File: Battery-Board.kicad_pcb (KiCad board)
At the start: 2 copper layers, 100 x 100 mm, 174 parts, among them J12 USB_C_Receptacle_USB2.0_16P, J13 STM32-Prog-Header, Q1 CSD18563Q5A, Q2 CSD18563Q5A, Q3 CSD18563Q5A, SW3 RESET, SW4 SW_SPDT, U1 8MHz, U10 NTMFS4D0N08XT1G, U11 NTMFS4D0N08XT1G, U12 NTMFS4D0N08XT1G, U13 NTMFS4D0N08XT1G, U14 NTMFS4D0N08XT1G, U23 ACS723xLCTR-10AU, U24 ACS723xLCTR-10AU, U25 MCP6007, U26 MCP6007, U27 ACS723xLCTR-10AU, U28 MCP6007, U29 MCP6007, U3 STM32G491KEUx, U30 MCP6007, U31 MCP6007, U4 MCP2542FD-E/SN, U5 MCP9700AT-ETT, U6 MCP9700AT-ETT, U7 MCP9700AT-ETT

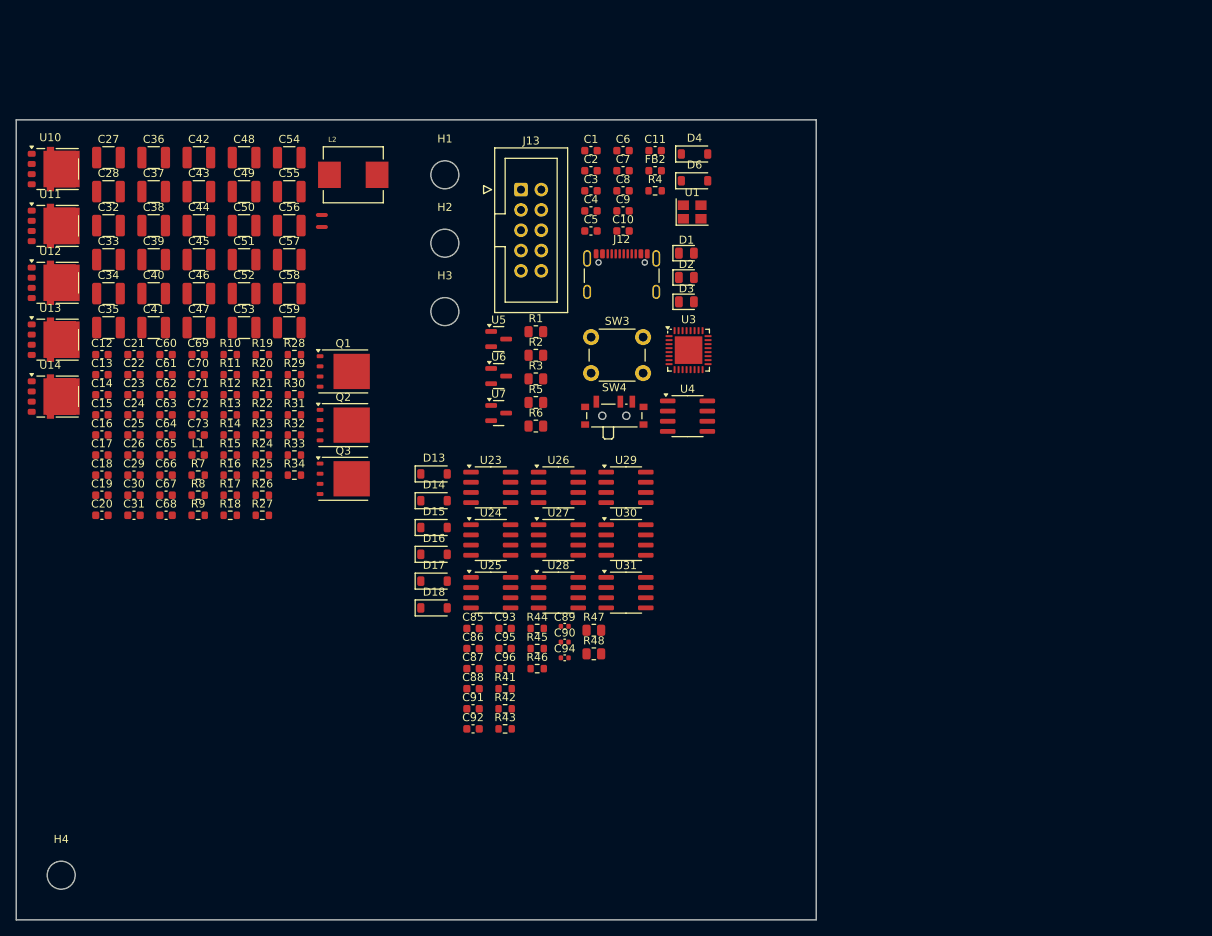
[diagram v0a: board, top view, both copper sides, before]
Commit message: Added missing symbols
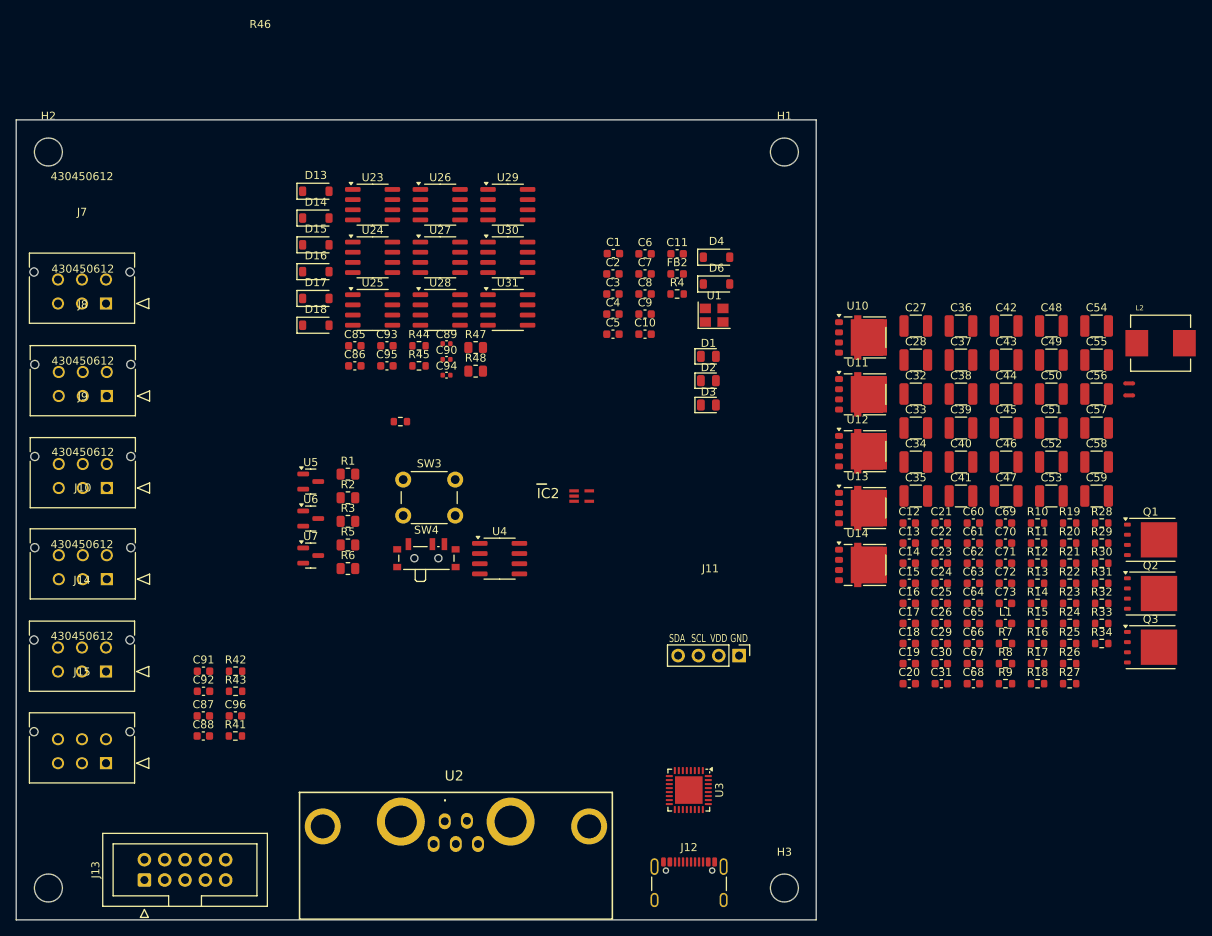
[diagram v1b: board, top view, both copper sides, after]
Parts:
- added IC2: ESDALC6V1W5, ecocad_lib_footprints:SOT65P210X110-5N, F.Cu at (158.6, 90.7)
- added J10: STD_PWR_HEADER, ecocad_lib_footprints:CON_430450612_MOL, F.Cu at (99.2, 101.1)
- added J11: OLED, ecocad_lib_footprints:Display_128x64_096_I2C, F.Cu at (174.4, 110.6)
- added J14: STD_PWR_HEADER, ecocad_lib_footprints:CON_430450612_MOL, F.Cu at (99.1, 112.6)
- added J15: STD_PWR_HEADER, ecocad_lib_footprints:CON_430450612_MOL, F.Cu at (99.1, 124.1)
- added J7: STD_PWR_HEADER, ecocad_lib_footprints:CON_430450612_MOL, F.Cu at (99.1, 66.6)
- added J8: STD_PWR_HEADER, ecocad_lib_footprints:CON_430450612_MOL, F.Cu at (99.2, 78.2)
- added J9: STD_PWR_HEADER, ecocad_lib_footprints:CON_430450612_MOL, F.Cu at (99.2, 89.7)
- added U2: ~, ecocad_lib_footprints:DB7W2-Male, F.Cu at (142.8, 133.0)
- moved L2 103.1 mm to (230.9, 71.6)
- moved Q1 103.1 mm to (229.7, 96.2)
- moved Q2 103.1 mm to (229.7, 102.9)
- moved Q3 103.1 mm to (229.7, 109.6)
- moved C42 103.1 mm to (211.6, 69.5)
- moved C43 103.1 mm to (211.6, 73.7)
- moved C44 103.1 mm to (211.6, 78.0)
- moved C45 103.1 mm to (211.6, 82.2)
- moved C46 103.1 mm to (211.6, 86.5)
- moved C47 103.1 mm to (211.6, 90.7)
- moved C48 103.1 mm to (217.3, 69.5)
- moved C49 103.1 mm to (217.3, 73.7)
- moved C50 103.1 mm to (217.3, 78.0)
- moved C51 103.1 mm to (217.3, 82.2)
- moved C52 103.1 mm to (217.3, 86.5)
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
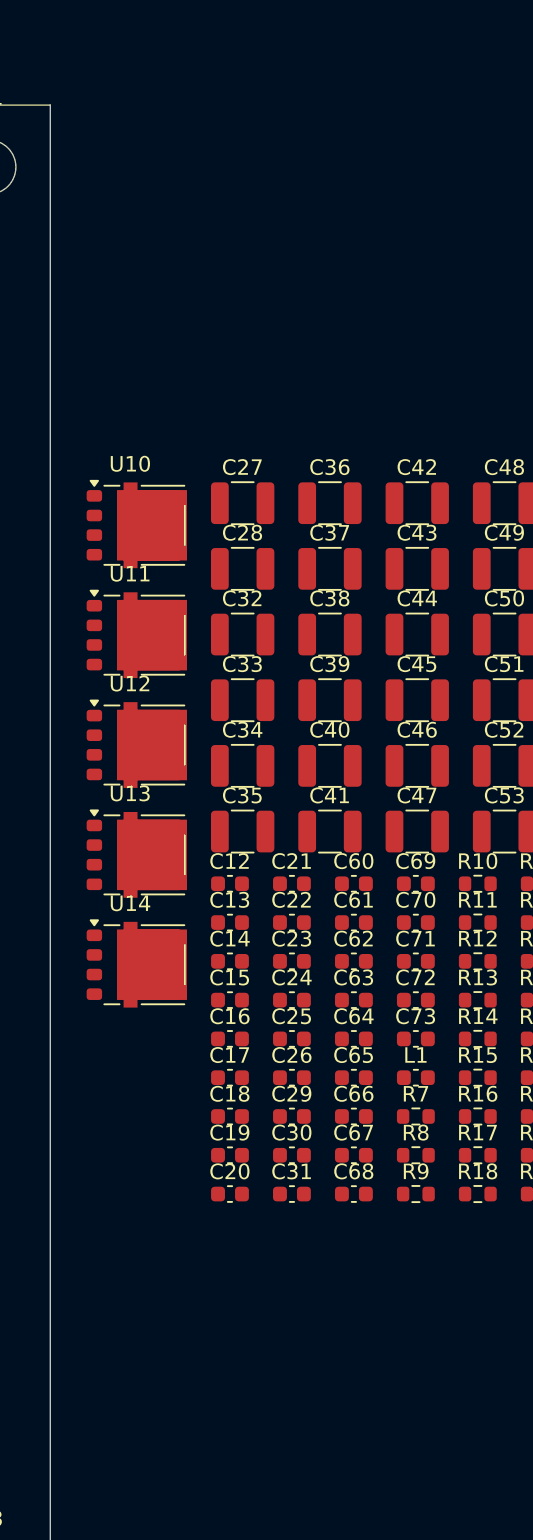
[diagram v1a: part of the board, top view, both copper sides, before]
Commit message: updated footprints for bucks and placement
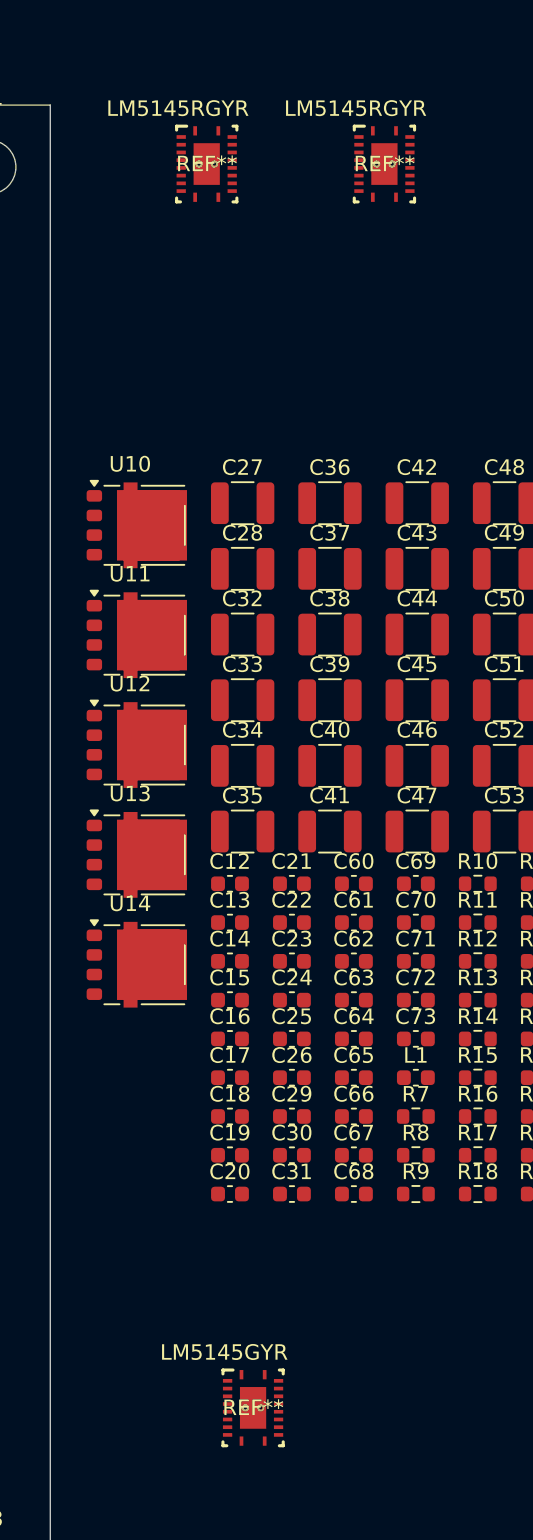
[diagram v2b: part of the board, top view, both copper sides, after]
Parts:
- added REF**: RGY0020B, ecocad_lib_footprints:RGY0020B, F.Cu at (201.0, 128.0)
- added REF**: RGY0020B, RGY0020B, F.Cu at (209.5, 47.5)
- added REF**: RGY0020B, RGY0020B, F.Cu at (198.0, 47.5)

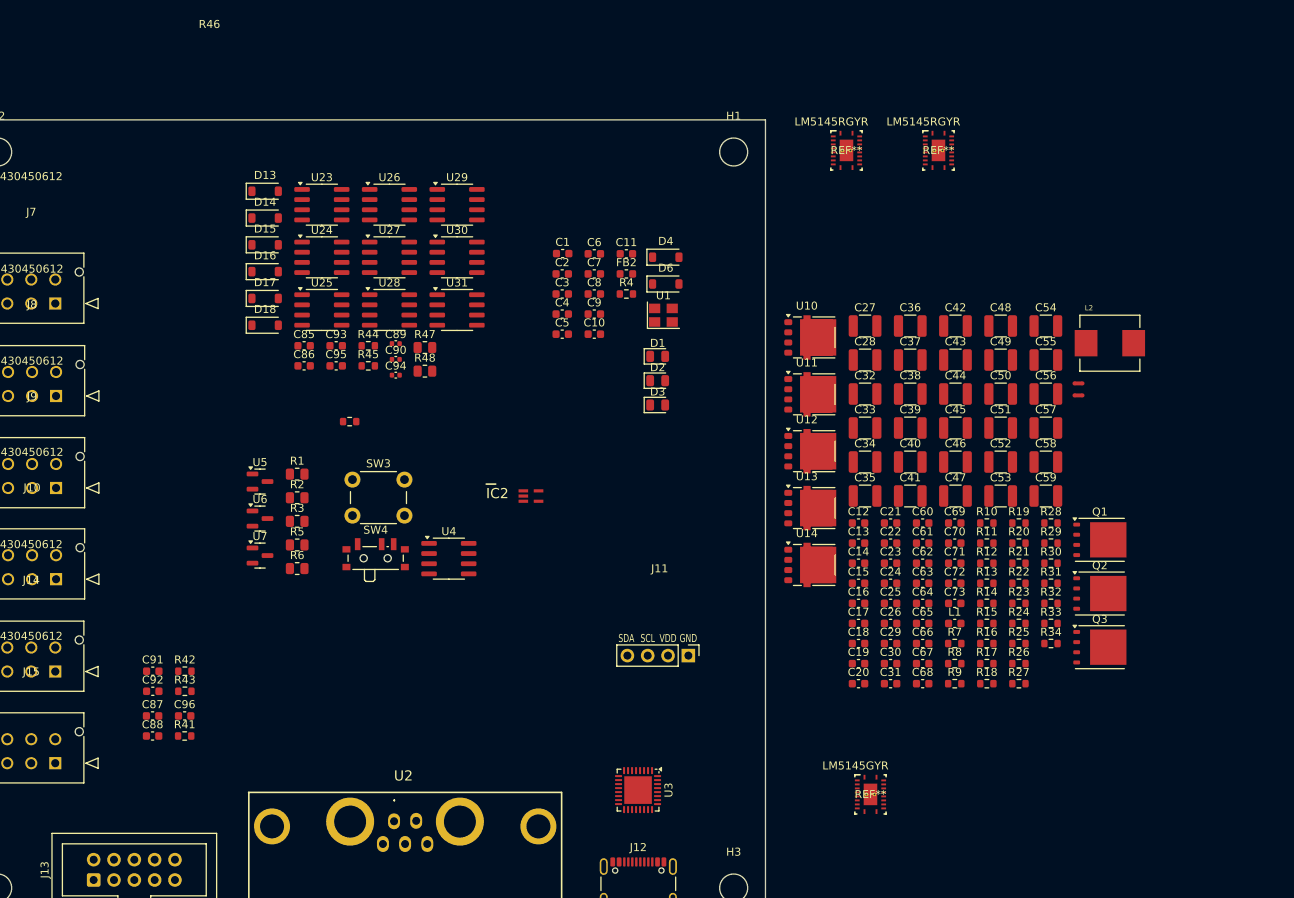
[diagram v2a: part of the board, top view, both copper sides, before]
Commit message: fixed footprints
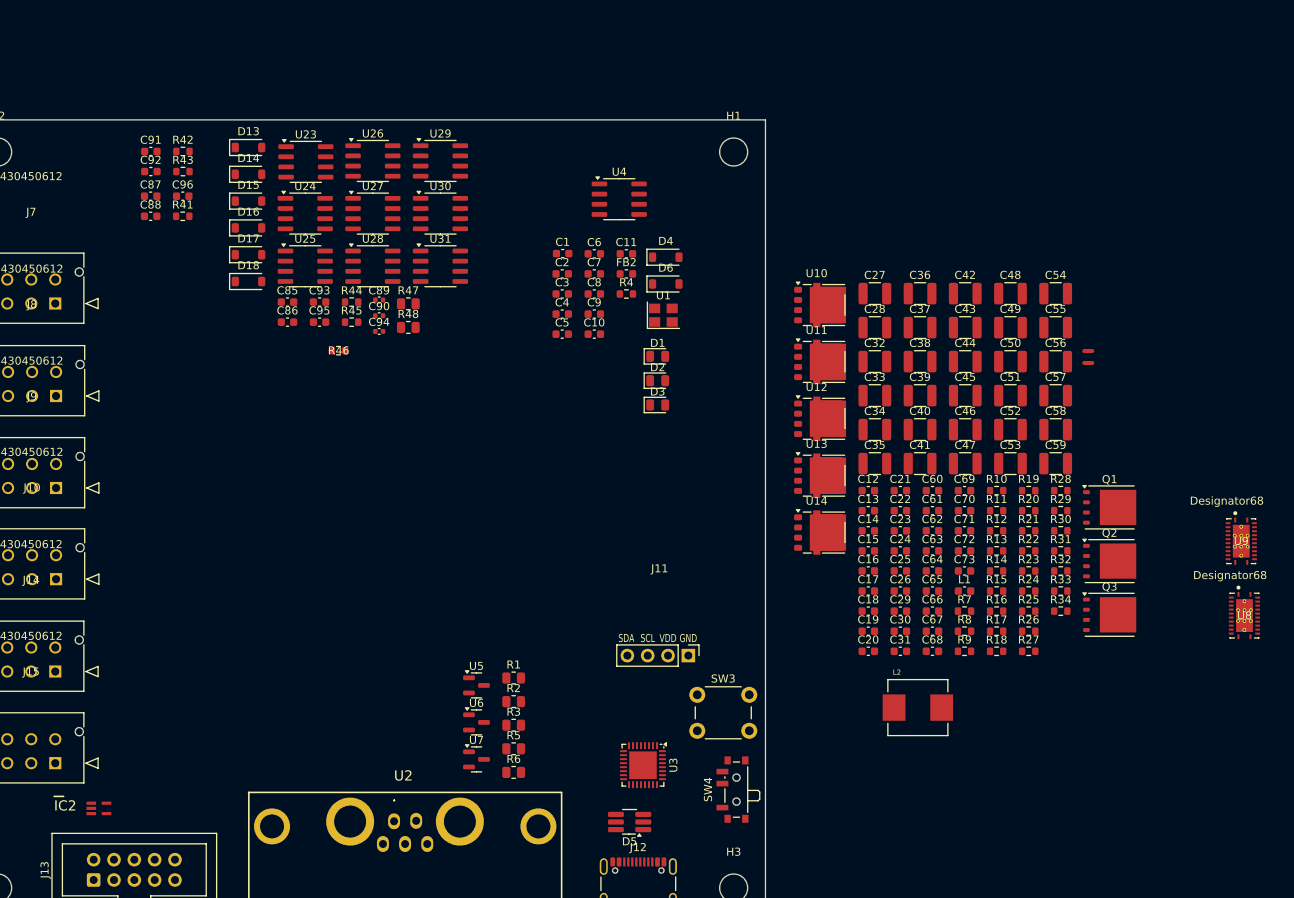
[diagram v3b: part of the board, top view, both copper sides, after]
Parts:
- removed REF**: RGY0020B, ecocad_lib_footprints:RGY0020B
- removed REF** (x2): RGY0020B, RGY0020B
- added D5: USBLC6-2SC6, Package_TO_SOT_SMD:TSOT-23-6_HandSoldering, F.Cu at (170.9, 131.4)
- added U8: LM5145, ecocad_lib_footprints:RGY0024F-MFG, F.Cu at (247.7, 105.7)
- added U9: LM5145, ecocad_lib_footprints:RGY0024F-MFG, F.Cu at (247.3, 96.4)
- moved IC2 66.6 mm to (104.5, 129.8)
- moved C87 65.0 mm to (111.0, 53.2)
- moved C88 65.0 mm to (111.0, 55.7)
- moved C91 65.0 mm to (111.0, 47.6)
- moved C92 65.0 mm to (111.0, 50.1)
- moved C96 65.0 mm to (115.0, 53.2)
- moved R41 65.0 mm to (115.0, 55.7)
- moved R42 65.0 mm to (115.1, 47.6)
- moved R43 65.0 mm to (115.1, 50.1)
- moved SW4 53.5 mm to (183.9, 127.4), turned to 90 degrees
- moved L2 51.5 mm to (206.9, 117.2)
- moved SW3 50.8 mm to (179.3, 115.5)
- moved U4 49.7 mm to (169.6, 53.6)
- moved R1 37.2 mm to (156.4, 113.5)
- moved R2 37.2 mm to (156.4, 116.4)
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
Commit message: updates on pcb layout
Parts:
- removed J10, J14, J15, J7, J8, J9: STD_PWR_HEADER, ecocad_lib_footprints:CON_430450612_MOL
- removed Q3: CSD18563Q5A, Package_TO_SOT_SMD:TDSON-8-1
- added U12: NTMFS4D0N08XT1G, ecocad_lib_footprints:PowerMosDFNHybrid, F.Cu at (155.5, 72.8)
- L1: footprint Capacitor_SMD:C_0603_1608Metric -> ecocad_lib_footprints:L_Bourns_SRR1208_12.7x12.7mm
- L2: footprint ecocad_lib_footprints:IND_SPM7054VC-220M-D -> ecocad_lib_footprints:L_Bourns_SRR1208_12.7x12.7mm
- U2: footprint ecocad_lib_footprints:DB7W2-Male -> ecocad_lib_footprints:DB7W2-30A
- moved U8 149.7 mm to (99.7, 82.9), turned to -90 degrees
- moved R1 142.4 mm to (34.6, 39.7)
- moved R2 142.4 mm to (34.6, 42.6)
- moved R3 142.4 mm to (34.6, 45.6)
- moved R5 142.4 mm to (34.6, 48.5)
- moved R6 142.4 mm to (34.6, 51.5)
- moved U5 142.4 mm to (29.9, 40.6)
- moved U6 142.4 mm to (29.9, 45.2)
- moved U7 142.4 mm to (29.9, 49.9)
- moved D5 139.1 mm to (36.8, 94.5)
- moved C54 119.5 mm to (110.5, 102.2), turned to 180 degrees
- moved C58 118.4 mm to (108.5, 57.3)
- moved C57 115.3 mm to (110.5, 98.0), turned to 180 degrees
- moved C53 115.0 mm to (108.5, 53.0)
- moved C42 113.7 mm to (110.5, 115.0), turned to 180 degrees
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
